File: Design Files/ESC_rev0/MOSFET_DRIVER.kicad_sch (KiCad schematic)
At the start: 38 parts, among them U2 DRV8302DCA

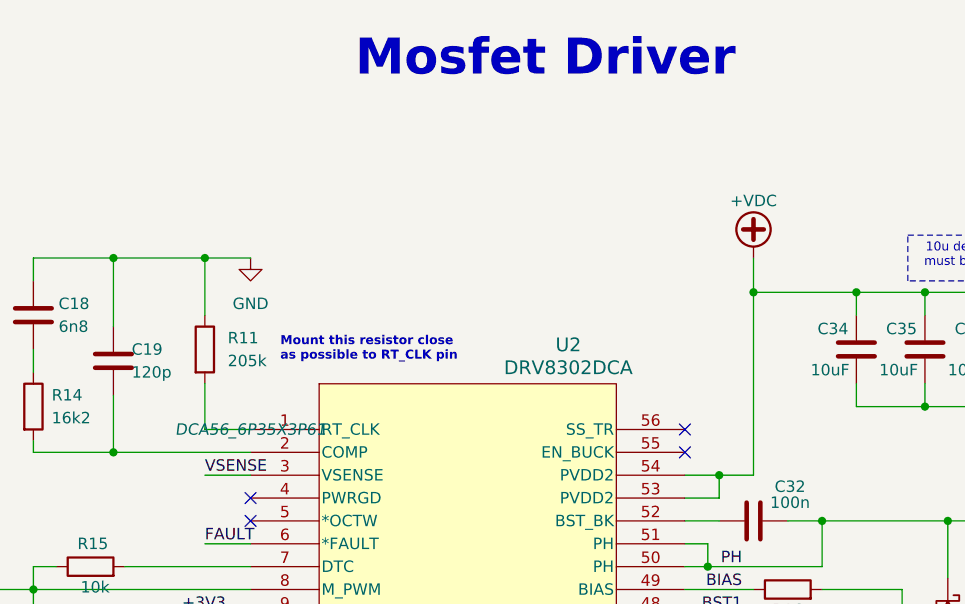
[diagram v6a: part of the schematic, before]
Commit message: update10
modifications to root page, completion of pages step_down and mechanical
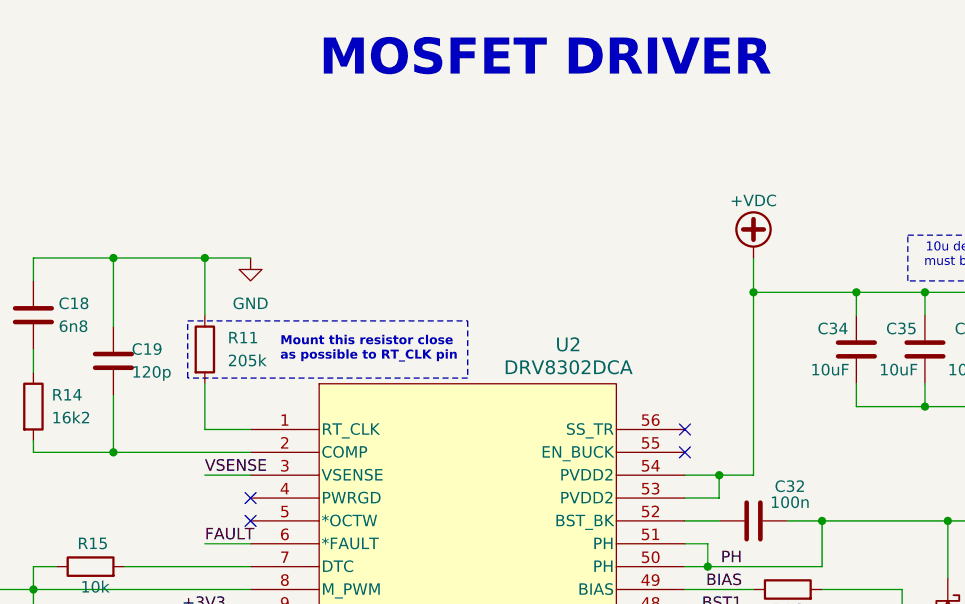
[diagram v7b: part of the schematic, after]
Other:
- title: Mosfet Driver -> MOSFET DRIVER
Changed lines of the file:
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@@
 	(paper "A4")
 	(title_block
-		(title "Mosfet Driver")
+		(title "MOSFET DRIVER")
 		(rev "0")
 	)
@@
 	)
 	(rectangle
+		(start 99.695 50.165)
+		(end 130.81 56.515)
+		(stroke
+			(width 0)
+			(type dash)
+		)
+		(fill
+			(type none)
+		)
+	)
+	(rectangle
 		(start 256.54 85.09)
 		(end 281.94 99.695)
@@
 					(italic yes)
 				)
+				(hide yes)
 			)
 		)

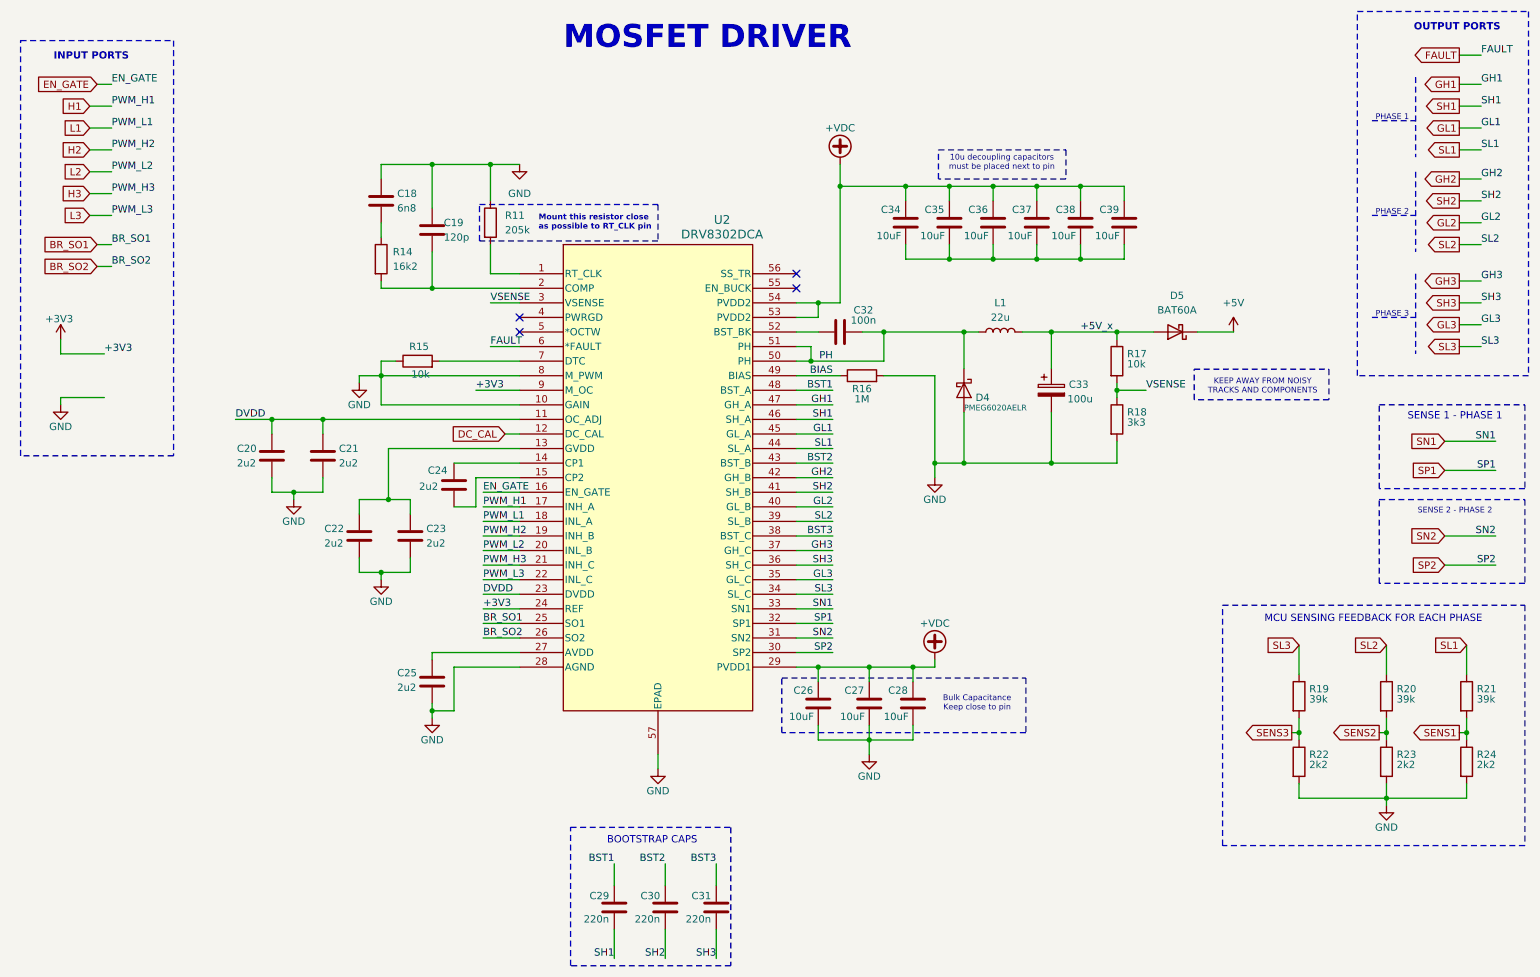
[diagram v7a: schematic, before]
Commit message: UPDATE 12
started schematics revision: edit and added info and circuits to some pages and assigned some footprints for components
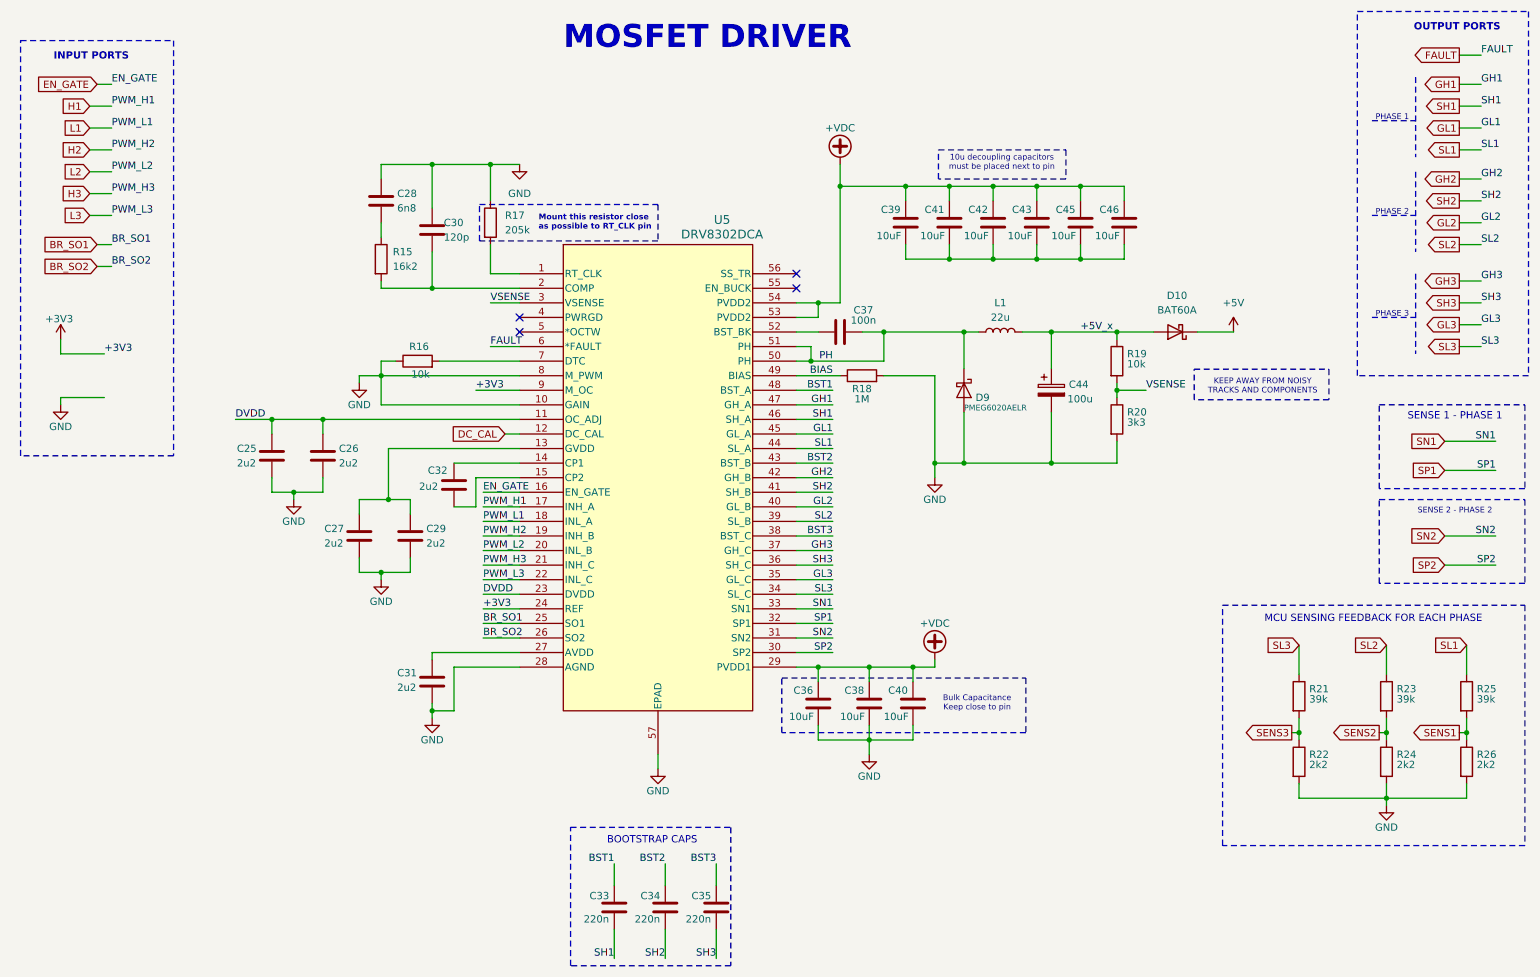
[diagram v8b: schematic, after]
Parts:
- C25: renamed from C20; footprint (none) -> Capacitor_SMD:C_0201_0603Metric
- C26: renamed from C21; footprint (none) -> Capacitor_SMD:C_0201_0603Metric
- C27: renamed from C22; footprint (none) -> Capacitor_SMD:C_0201_0603Metric
- C28: renamed from C18; footprint (none) -> Capacitor_SMD:C_0201_0603Metric
- C29: renamed from C23; footprint (none) -> Capacitor_SMD:C_0201_0603Metric
- C30: renamed from C19; footprint (none) -> Capacitor_SMD:C_0201_0603Metric
- C31: renamed from C25; footprint (none) -> Capacitor_SMD:C_0201_0603Metric
- C32: renamed from C24; footprint (none) -> Capacitor_SMD:C_0201_0603Metric
- C33: renamed from C29; footprint (none) -> Capacitor_SMD:C_0201_0603Metric
- C34: renamed from C30; footprint (none) -> Capacitor_SMD:C_0201_0603Metric
- C35: renamed from C31; footprint (none) -> Capacitor_SMD:C_0201_0603Metric
- C36: renamed from C26; footprint (none) -> Capacitor_SMD:C_0201_0603Metric
- C37: renamed from C32; footprint (none) -> Capacitor_SMD:C_0201_0603Metric
- C38: renamed from C27; footprint (none) -> Capacitor_SMD:C_0201_0603Metric
- C39: renamed from C34; footprint (none) -> Capacitor_SMD:C_0201_0603Metric
- C40: renamed from C28; footprint (none) -> Capacitor_SMD:C_0201_0603Metric
- C41: renamed from C35; footprint (none) -> Capacitor_SMD:C_0201_0603Metric
- C42: renamed from C36; footprint (none) -> Capacitor_SMD:C_0201_0603Metric
- C43: renamed from C37; footprint (none) -> Capacitor_SMD:C_0201_0603Metric
- C44: renamed from C33; footprint (none) -> Capacitor_SMD:C_0201_0603Metric
- C45: renamed from C38; footprint (none) -> Capacitor_SMD:C_0201_0603Metric
- C46: renamed from C39; footprint (none) -> Capacitor_SMD:C_0201_0603Metric
- U5: renamed from U2; footprint DCA56_6P35X3P61 -> DRV8302DCA_foot:DCA56_6P35X3P61
- renumbered D5 to D10, D4 to D9, R14 to R15, R15 to R16, R11 to R17, R16 to R18, R17 to R19, R18 to R20, R19 to R21, R20 to R23, R23 to R24, R21 to R25, R24 to R26
